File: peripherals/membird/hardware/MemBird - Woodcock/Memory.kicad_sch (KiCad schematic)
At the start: 4 parts, among them U1 AS6C8016, U16 AS6C8016, U17 AS6C8016, U3 AS6C8016

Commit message: MemBird - Woodcock Rev.1 Schematic is complete
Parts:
- renumbered U1 to U16, U3 to U17, U16 to U18, U17 to U19
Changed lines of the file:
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@@
 		(on_board yes)
 		(dnp no)
-		(property "Reference" "#PWR04"
+		(property "Reference" "#PWR072"
 			(at 57.15 105.41 0)
 			(effects
@@
 			(project "MemBird - Woodcock"
 				(path "/6376137f-dc27-4ca5-b911-07fd12a37fc2/2607bc31-0c18-4e05-9a61-cf4e6196c75a"
-					(reference "#PWR04")
+					(reference "#PWR072")
 					(unit 1)
 				)
@@
 		(on_board yes)
 		(dnp no)
-		(property "Reference" "#PWR022"
+		(property "Reference" "#PWR076"
 			(at 129.54 105.41 0)
 			(effects
@@
 			(project "MemBird - Woodcock"
 				(path "/6376137f-dc27-4ca5-b911-07fd12a37fc2/2607bc31-0c18-4e05-9a61-cf4e6196c75a"
-					(reference "#PWR022")
+					(reference "#PWR076")
 					(unit 1)
 				)
@@
 		(on_board yes)
 		(dnp no)
-		(property "Reference" "U17"
+		(property "Reference" "U19"
 			(at 120.396 118.11 0)
 			(effects
@@
 			(project "MemBird - Woodcock"
 				(path "/6376137f-dc27-4ca5-b911-07fd12a37fc2/2607bc31-0c18-4e05-9a61-cf4e6196c75a"
-					(reference "U17")
+					(reference "U19")
 					(unit 1)
 				)
@@
 		(on_board yes)
 		(dnp no)
-		(property "Reference" "U1"
+		(property "Reference" "U16"
 			(at 48.006 38.1 0)
 			(effects
@@
 			(project "MemBird - Woodcock"
 				(path "/6376137f-dc27-4ca5-b911-07fd12a37fc2/2607bc31-0c18-4e05-9a61-cf4e6196c75a"
-					(reference "U1")
+					(reference "U16")
 					(unit 1)
 				)
@@
 		(on_board yes)
 		(dnp no)
-		(property "Reference" "U16"
+		(property "Reference" "U18"
 			(at 120.396 38.1 0)
 			(effects
@@
 			(project "MemBird - Woodcock"
 				(path "/6376137f-dc27-4ca5-b911-07fd12a37fc2/2607bc31-0c18-4e05-9a61-cf4e6196c75a"
-					(reference "U16")
+					(reference "U18")
 					(unit 1)
 				)
@@
 		(on_board yes)
 		(dnp no)
-		(property "Reference" "#PWR03"
+		(property "Reference" "#PWR075"
 			(at 129.54 40.64 0)
 			(effects
@@
 			(project "MemBird - Woodcock"
 				(path "/6376137f-dc27-4ca5-b911-07fd12a37fc2/2607bc31-0c18-4e05-9a61-cf4e6196c75a"
-					(reference "#PWR03")
+					(reference "#PWR075")
 					(unit 1)
 				)
@@
 		(on_board yes)
 		(dnp no)
-		(property "Reference" "#PWR021"
+		(property "Reference" "#PWR073"
 			(at 57.15 120.65 0)
 			(effects
@@
 			(project "MemBird - Woodcock"
 				(path "/6376137f-dc27-4ca5-b911-07fd12a37fc2/2607bc31-0c18-4e05-9a61-cf4e6196c75a"
-					(reference "#PWR021")
+					(reference "#PWR073")
 					(unit 1)
 				)
@@
 		(on_board yes)
 		(dnp no)
-		(property "Reference" "#PWR06"
+		(property "Reference" "#PWR074"
 			(at 57.15 185.42 0)
 			(effects
@@
 			(project "MemBird - Woodcock"
 				(path "/6376137f-dc27-4ca5-b911-07fd12a37fc2/2607bc31-0c18-4e05-9a61-cf4e6196c75a"
-					(reference "#PWR06")
+					(reference "#PWR074")
 					(unit 1)
 				)
@@
 		(on_board yes)
 		(dnp no)
-		(property "Reference" "#PWR05"
+		(property "Reference" "#PWR077"
 			(at 129.54 120.65 0)
 			(effects
@@
 			(project "MemBird - Woodcock"
 				(path "/6376137f-dc27-4ca5-b911-07fd12a37fc2/2607bc31-0c18-4e05-9a61-cf4e6196c75a"
-					(reference "#PWR05")
+					(reference "#PWR077")
 					(unit 1)
 				)
@@
 		(on_board yes)
 		(dnp no)
-		(property "Reference" "U3"
+		(property "Reference" "U17"
 			(at 48.006 118.11 0)
 			(effects
@@
 			(project "MemBird - Woodcock"
 				(path "/6376137f-dc27-4ca5-b911-07fd12a37fc2/2607bc31-0c18-4e05-9a61-cf4e6196c75a"
-					(reference "U3")
+					(reference "U17")
 					(unit 1)
 				)
@@
 		(on_board yes)
 		(dnp no)
-		(property "Reference" "#PWR051"
+		(property "Reference" "#PWR078"
 			(at 129.54 185.42 0)
 			(effects
@@
 			(project "MemBird - Woodcock"
 				(path "/6376137f-dc27-4ca5-b911-07fd12a37fc2/2607bc31-0c18-4e05-9a61-cf4e6196c75a"
-					(reference "#PWR051")
+					(reference "#PWR078")
 					(unit 1)
 				)
@@
 		(on_board yes)
 		(dnp no)
-		(property "Reference" "#PWR052"
+		(property "Reference" "#PWR071"
 			(at 57.15 40.64 0)
 			(effects
@@
 			(project ""
 				(path "/6376137f-dc27-4ca5-b911-07fd12a37fc2/2607bc31-0c18-4e05-9a61-cf4e6196c75a"
-					(reference "#PWR052")
-					(unit 1)
-				)
+					(reference "#PWR071")
+					(unit 1)
+				)

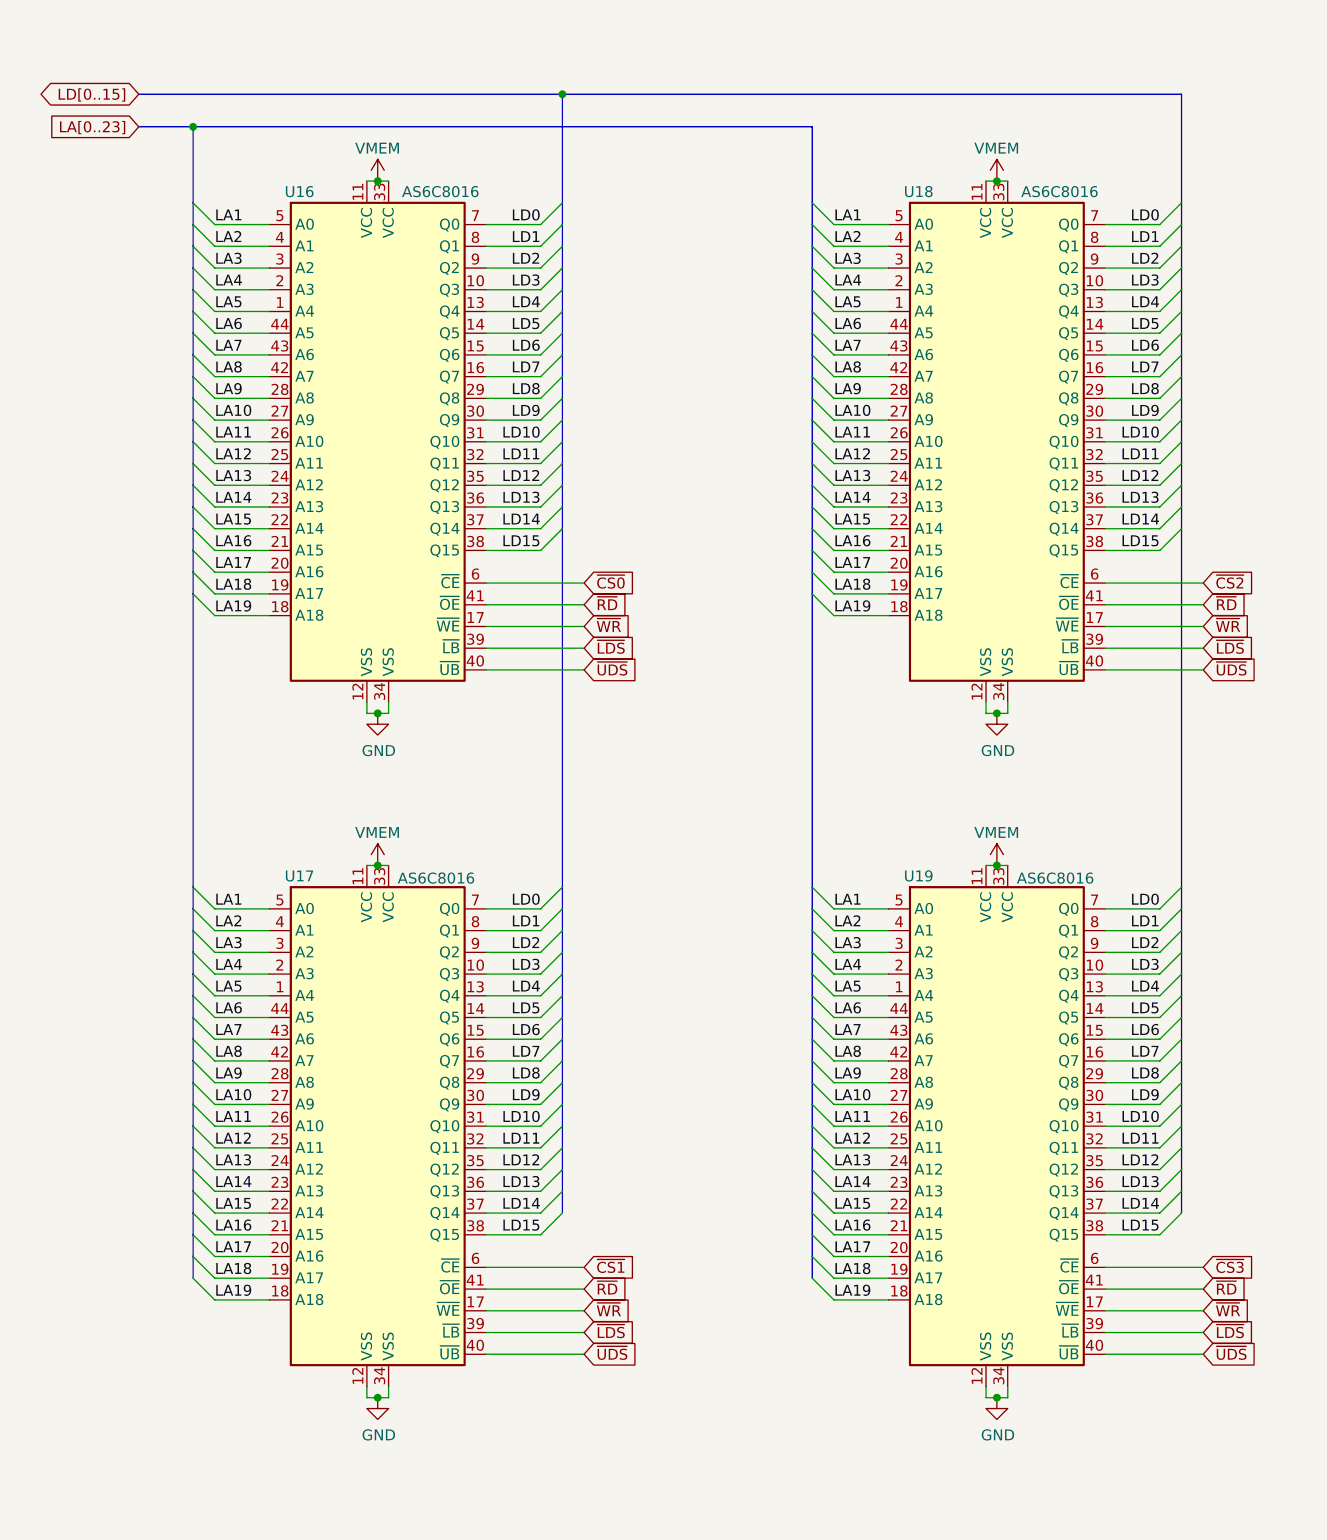
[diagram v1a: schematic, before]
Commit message: Finished the MemBird - Woodcock 16-bit memory board layout
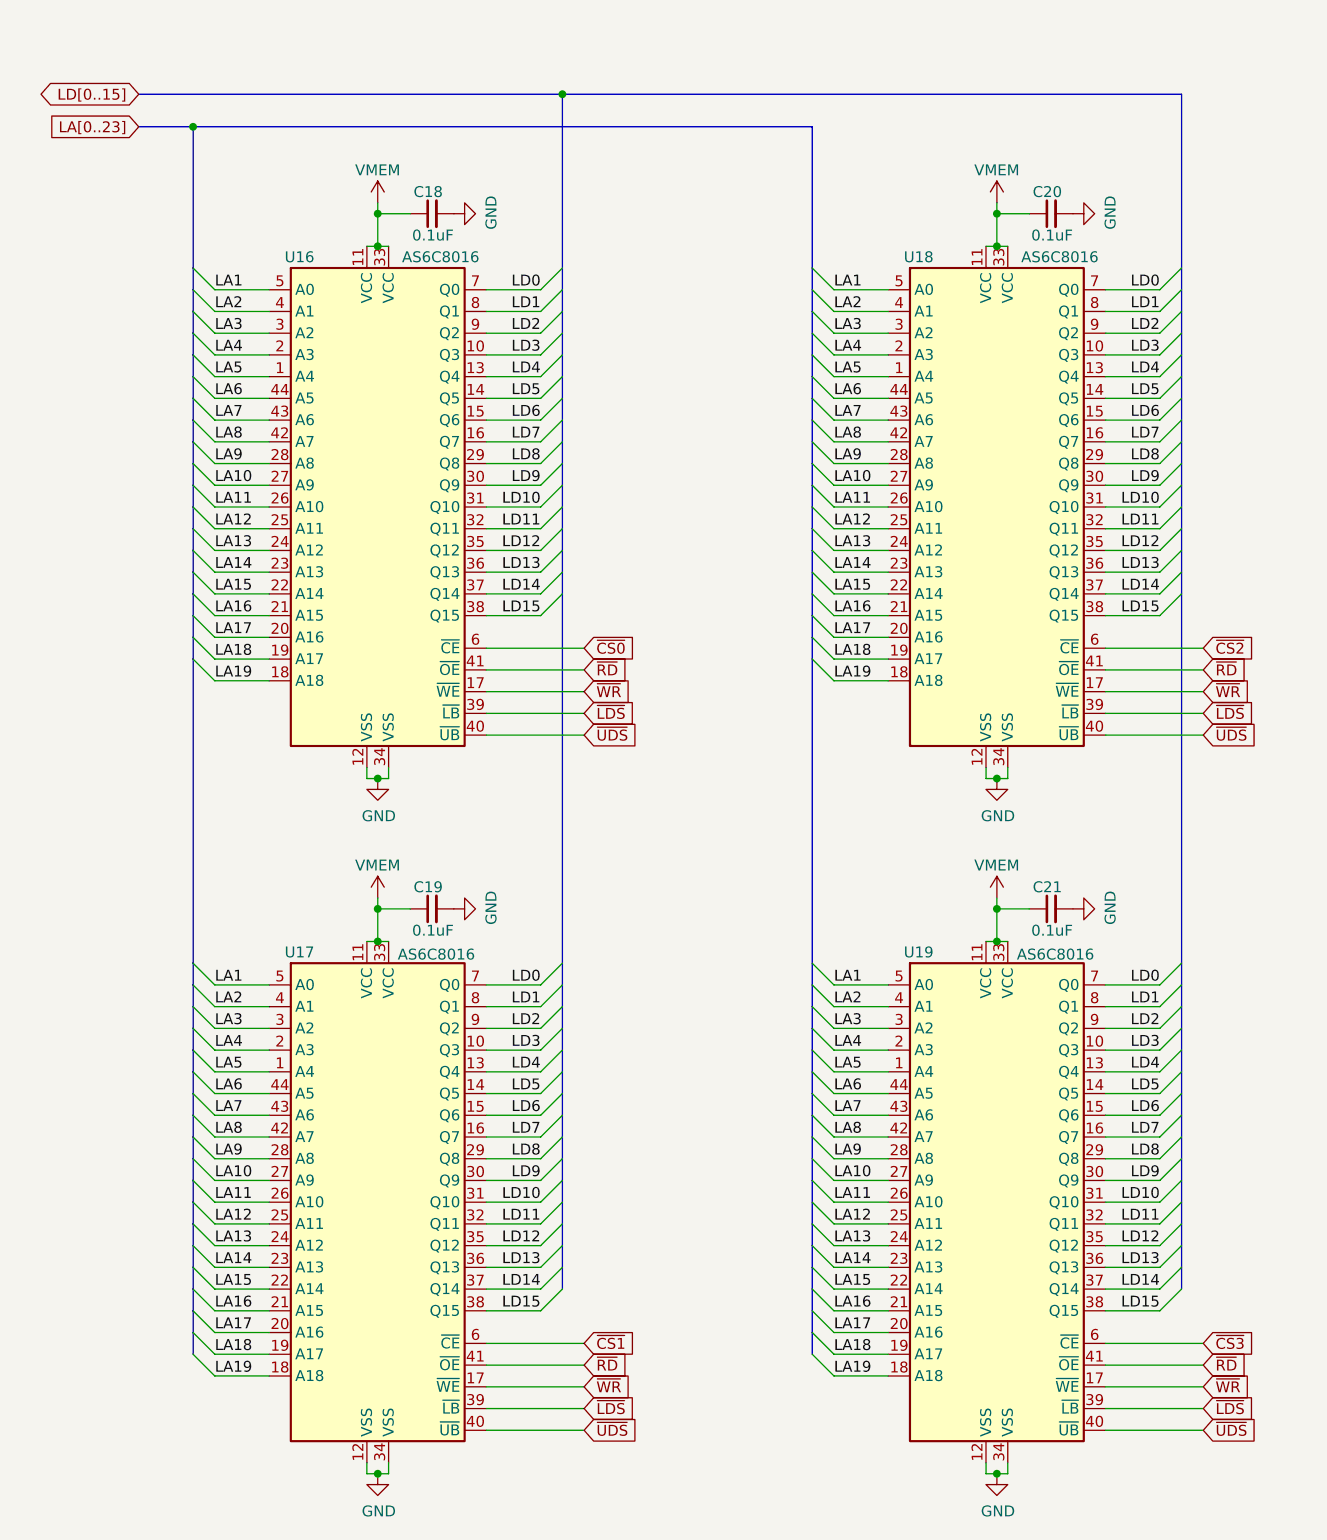
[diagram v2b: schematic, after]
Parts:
- added C18, C19, C20, C21: 0.1uF, Capacitor_SMD:C_0805_2012Metric_Pad1.18x1.45mm_HandSolder, symbol Device:C_Small
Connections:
- net GND: now also C18.2, C19.2, C20.2, C21.2
- net VMEM: now also C18.1, C19.1, C20.1, C21.1
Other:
- moved on the sheet: U16, U17, U18, U19

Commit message: k30p-VME rev.1, MemBird Woodcock rev.1, and frontpanels
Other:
- moved on the sheet: C18, C19, C20, C21, U16, U17, U18, U19
